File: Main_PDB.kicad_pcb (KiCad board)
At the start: 4 copper layers, 210.1 x 206 mm, 134 parts, among them Q4 NMOS, Q5 NMOS, Q6 NMOS, Q7 NMOS, Q8 NMOS, U10 ACS758LCB-100U-PFF-T, U11 ACS758LCB-100U-PFF-T, U12 ACS758LCB-100U-PFF-T, U2 LM5148RGYR, U3 LMR36015ARNXR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

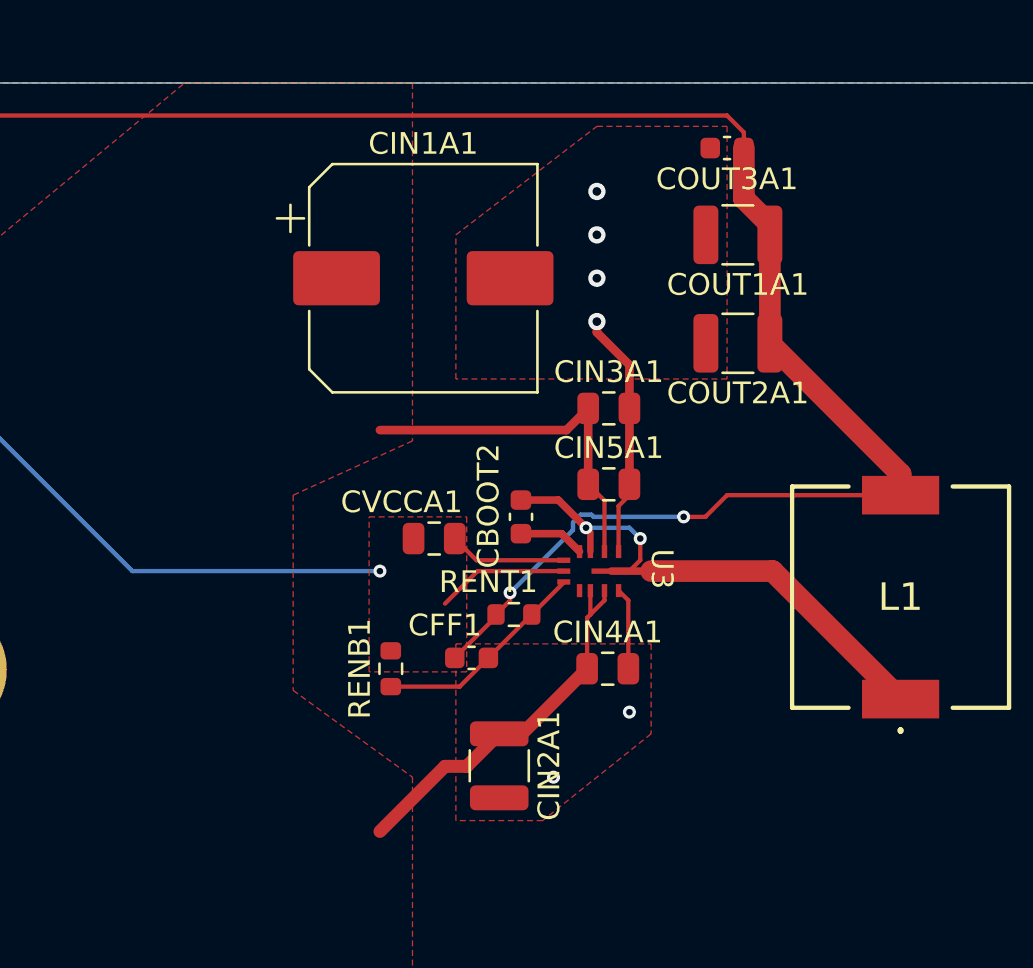
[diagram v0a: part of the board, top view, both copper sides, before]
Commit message: redid 3.3 buck layout on pcb
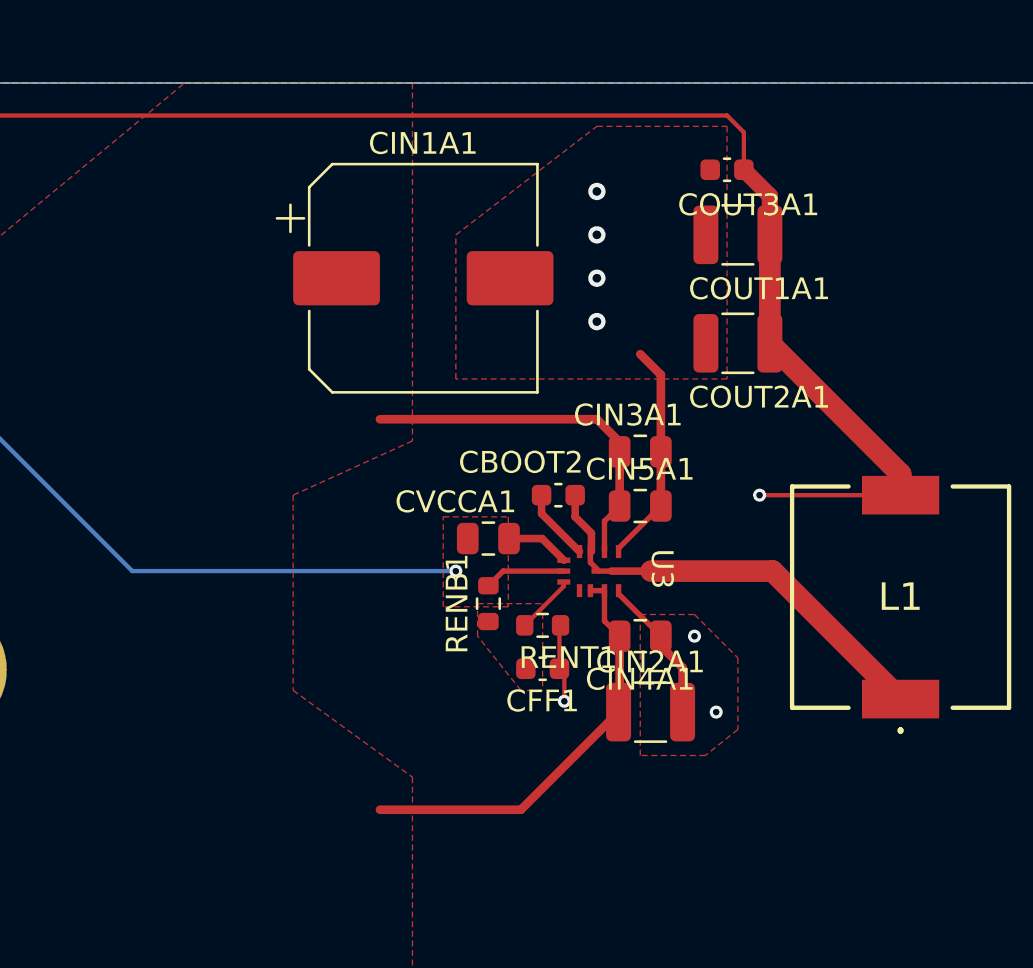
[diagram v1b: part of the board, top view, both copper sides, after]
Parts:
- moved CIN2A1 7.40 mm to (491.5, 73.0), turned to 0 degrees
- moved RENB1 5.41 mm to (484.0, 68.0)
- moved CFF1 3.31 mm to (486.5, 71.0), turned to 180 degrees
- moved CVCCA1 2.50 mm to (484.0, 65.0)
- moved CIN3A1 2.47 mm to (491.0, 61.0)
- moved CIN4A1 2.12 mm to (491.0, 69.5)
- moved CBOOT2 1.99 mm to (487.2, 63.0), turned to 0 degrees
- moved CIN5A1 1.76 mm to (491.0, 63.5)
- moved RENT1 1.42 mm to (486.5, 69.0), turned to 180 degrees
- moved COUT3A1 1.00 mm to (495.0, 48.0)
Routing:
- net Net-(U3-FB): track 9.99 -> 3.06 mm
- net Net-(U3-NC): track 25.7 -> 21.2 mm, vias 2 -> 0
- net +3.3V: track 91.2 -> 94.4 mm
- net Net-(U3-VCC): track 5.44 -> 2.94 mm
- net PGND: track 15.2 -> 17.1 mm
- net /48V_MAIN: track 34.6 -> 36.2 mm
- net AGND: track 47.1 -> 48.3 mm
- added copper zone on F.Cu, net Net-(U3-FB)

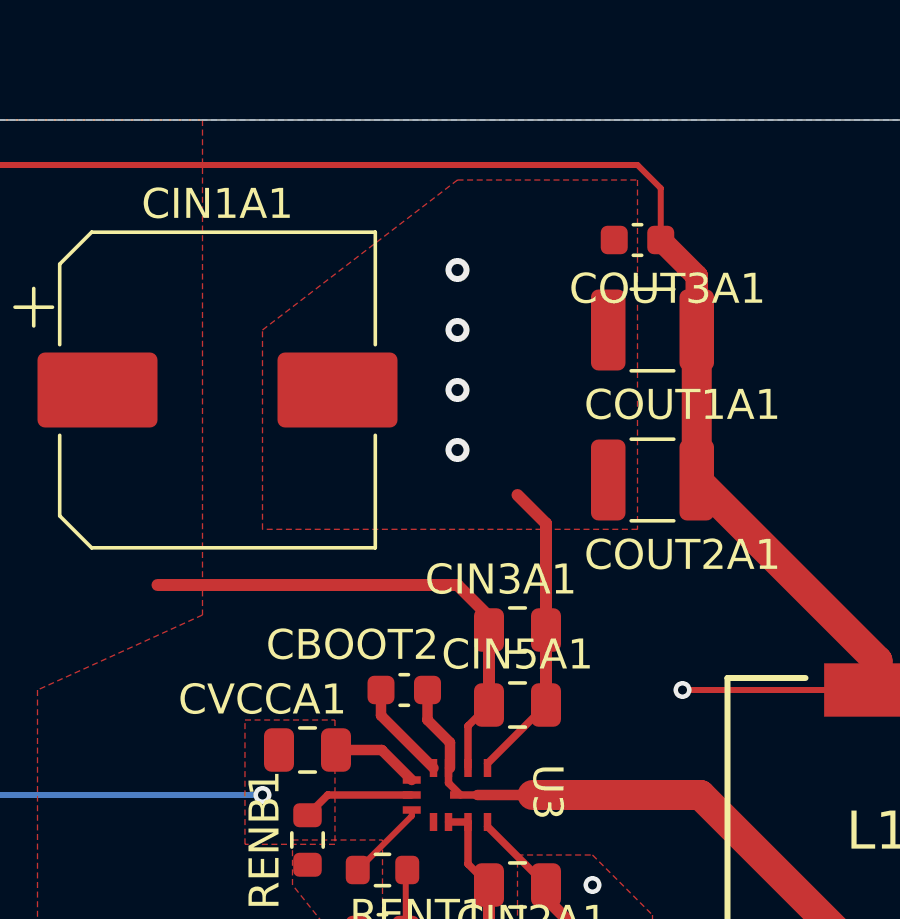
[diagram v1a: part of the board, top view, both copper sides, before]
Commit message: edited pgnd (upper) on 3.3V buck
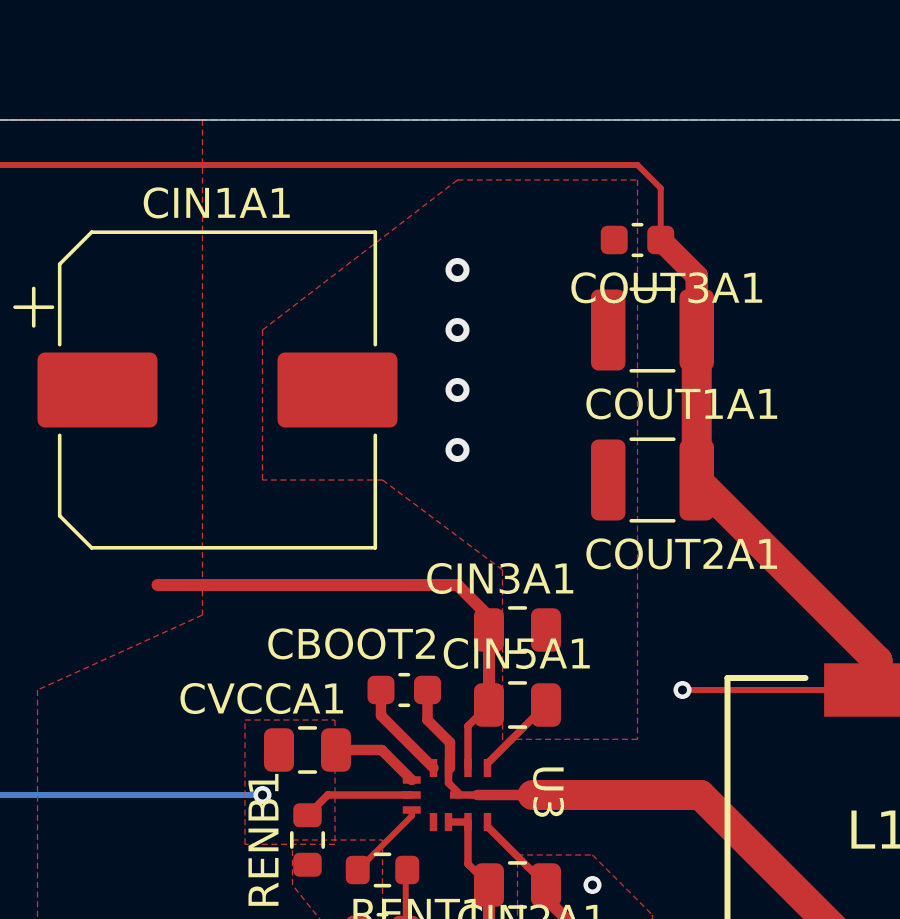
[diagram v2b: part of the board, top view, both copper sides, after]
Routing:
- net PGND: track 17.1 -> 9.73 mm
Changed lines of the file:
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@@
-	)
-	(segment
-		(start 491.95 63.5)
-		(end 491.95 61)
-		(width 0.4)
-		(layer "F.Cu")
-		(net "PGND")
-	)
-	(segment
-		(start 491.95 57.45)
-		(end 491 56.5)
-		(width 0.4)
-		(layer "F.Cu")
-		(net "PGND")
 	)
 	(segment
@@
 	)
 	(segment
-		(start 491.95 61)
-		(end 491.95 57.45)
-		(width 0.4)
-		(layer "F.Cu")
-		(net "PGND")
-	)
-	(segment
 		(start 492.95 70.95)
 		(end 492.95 73)
@@
 		(polygon
 			(pts
-				(xy 495 57.644416) (xy 482.5 57.644416) (xy 482.5 51) (xy 489 46) (xy 495 46)
-			)
-		)
+				(xy 495 64.644416) (xy 490.5 64.644416) (xy 490.504562 64.63794) (xy 490.5 59) (xy 486.5 56) (xy 482.5 56)
+				(xy 482.5 51) (xy 489 46) (xy 495 46)
+			)
+		)

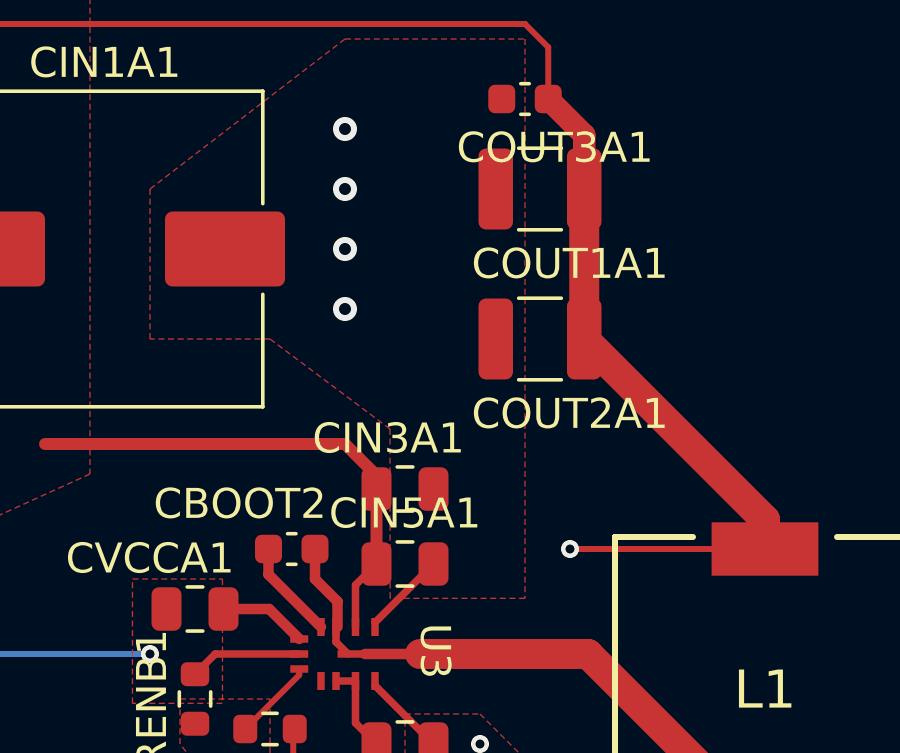
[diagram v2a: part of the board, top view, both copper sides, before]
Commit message: added additonal vias in pgnd pour
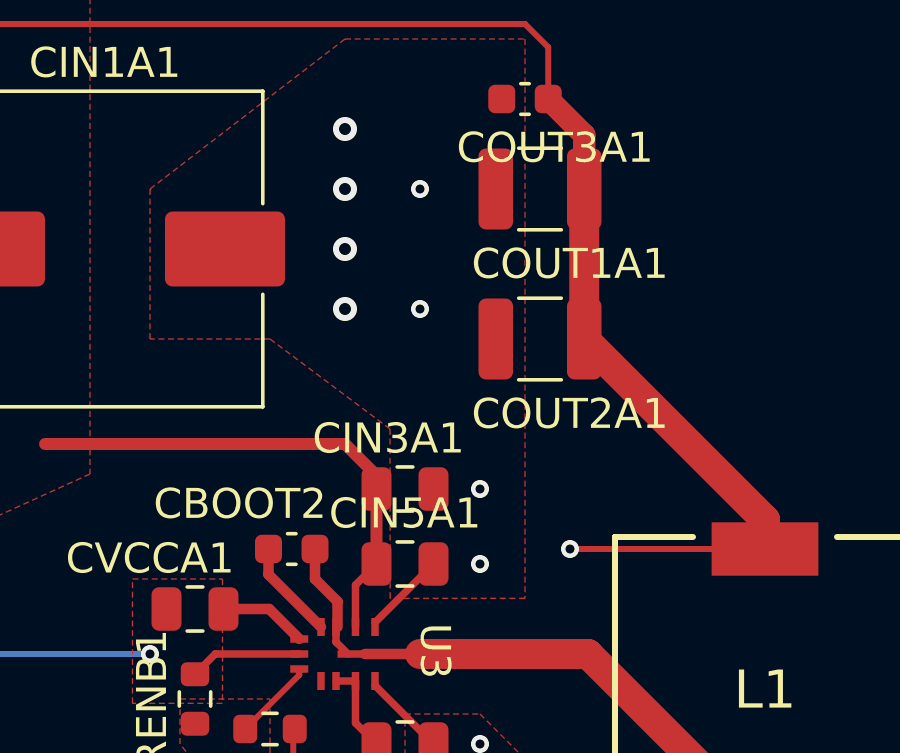
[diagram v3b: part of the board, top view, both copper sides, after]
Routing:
- net PGND: vias 36 -> 40
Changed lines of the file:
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@@
+	)
+	(via
+		(at 491.5 51)
+		(size 0.6)
+		(drill 0.3)
+		(layers "F.Cu" "B.Cu")
+		(free yes)
+		(net "PGND")
 	)
 	(via
@@
 	)
 	(via
+		(at 493.5 61)
+		(size 0.6)
+		(drill 0.3)
+		(layers "F.Cu" "B.Cu")
+		(free yes)
+		(net "PGND")
+	)
+	(via
 		(at 396.5 57.5)
 		(size 1)
@@
 		(size 1)
 		(drill 0.5)
+		(layers "F.Cu" "B.Cu")
+		(free yes)
+		(net "PGND")
+	)
+	(via
+		(at 493.5 63.5)
+		(size 0.6)
+		(drill 0.3)
 		(layers "F.Cu" "B.Cu")
 		(free yes)
@@
 		(layers "F.Cu" "B.Cu")
 		(free yes)
+		(net "PGND")
+	)
+	(via
+		(at 491.5 55)
+		(size 0.6)
+		(drill 0.3)
+		(layers "F.Cu" "B.Cu")
+		(free yes)

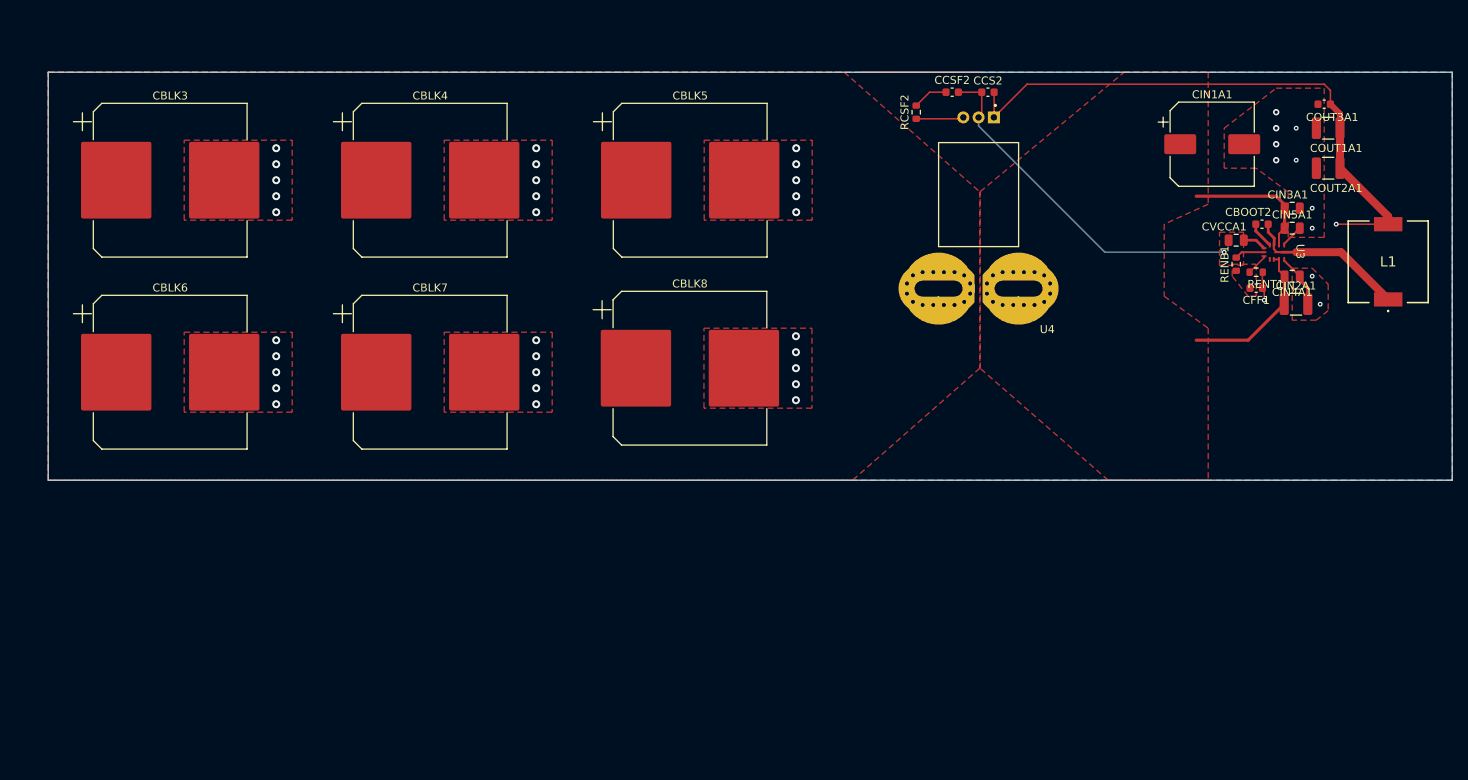
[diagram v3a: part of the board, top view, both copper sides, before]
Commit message: bulk caps relayout and added power pours on bottom layer
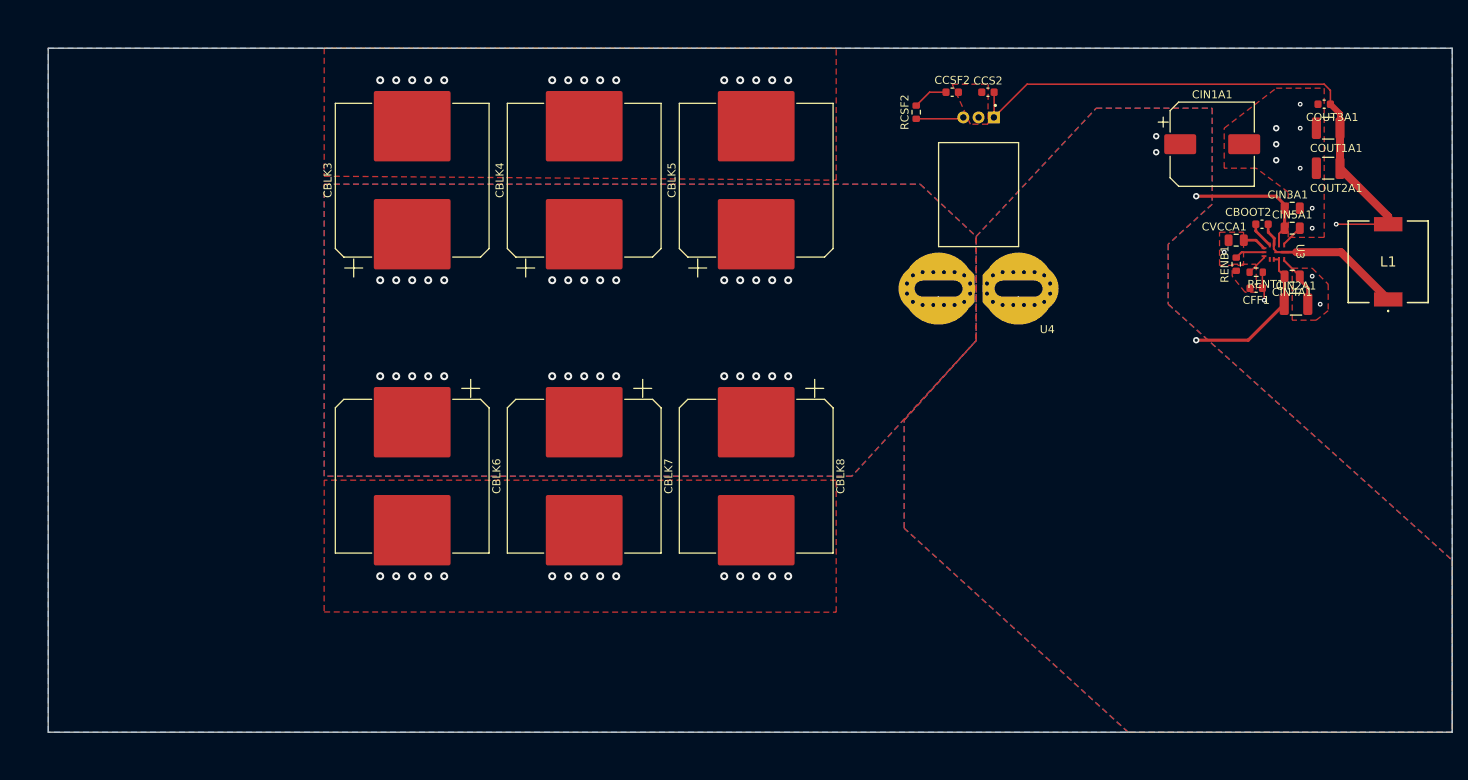
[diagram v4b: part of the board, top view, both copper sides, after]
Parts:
- moved CBLK6 32.9 mm to (381.0, 94.5), turned to -90 degrees
- moved CBLK3 30.2 mm to (381.0, 57.5), turned to 90 degrees
- moved CBLK7 23.2 mm to (402.5, 94.5), turned to -90 degrees
- moved CBLK4 19.2 mm to (402.5, 57.5), turned to 90 degrees
- moved CBLK8 15.8 mm to (424.0, 94.5), turned to -90 degrees
- moved CBLK5 8.25 mm to (424.0, 57.5), turned to 90 degrees
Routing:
- net AGND: track 48.3 -> 42.6 mm
- net /48V_PRECH: vias 0 -> 30
- net /48V_MAIN: vias 0 -> 4
- added copper zone on B.Cu, net /48V_MAIN
- added copper zone on B.Cu, net /48V_PRECH
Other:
- board size 210.1 x 206 mm -> 210.1 x 209 mm

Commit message: silkscreen updates
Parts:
- moved U5 88.4 mm to (133.8, 93.2)
- renumbered CIN4A1 to CHF4A1
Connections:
- CBLK3 pad 2: PGND -> AGND
- CBLK4 pad 2: PGND -> AGND
- CBLK5 pad 2: PGND -> AGND
- CBLK6 pad 2: PGND -> AGND
- CBLK7 pad 2: PGND -> AGND
- CBLK8 pad 2: PGND -> AGND
- CBLKA1 pad 2: PGND -> AGND
- CBLKA2 pad 2: PGND -> AGND
- CBLKA3 pad 2: PGND -> AGND
- CBLKA4 pad 2: PGND -> AGND
- CBULK1 pad 2: PGND -> AGND
- CBULK2 pad 2: PGND -> AGND
- CHF4A1 pad 2: PGND -> AGND
- CIN1A1 pad 2: PGND -> AGND
- CIN1B1 pad 2: PGND -> AGND
- CIN1B2 pad 2: PGND -> AGND
- CIN2A1 pad 2: PGND -> AGND
- CIN2B1 pad 1: PGND -> AGND
- CIN2B2 pad 1: PGND -> AGND
- CIN3A1 pad 2: PGND -> AGND
- CIN3B1 pad 1: PGND -> AGND
- CIN3B2 pad 1: PGND -> AGND
- CIN4B1 pad 1: PGND -> AGND
- CIN4B2 pad 1: PGND -> AGND
- CIN5A1 pad 2: PGND -> AGND
- CIN5B1 pad 1: PGND -> AGND
- CIN5B2 pad 1: PGND -> AGND
- CINC1 pad 1: PGND -> AGND
- CINC10 pad 2: PGND -> AGND
- CINC11 pad 2: PGND -> AGND
- CINC12 pad 2: PGND -> AGND
- CINC2 pad 1: PGND -> AGND
- CINC3 pad 1: PGND -> AGND
- CINC4 pad 1: PGND -> AGND
- CINC5 pad 1: PGND -> AGND
- CINC6 pad 1: PGND -> AGND
- CINC7 pad 1: PGND -> AGND
- CINC8 pad 1: PGND -> AGND
- CINC9 pad 2: PGND -> AGND
- COUT1A1 pad 2: PGND -> AGND
- COUT1B1 pad 2: PGND -> AGND
- COUT1B2 pad 2: PGND -> AGND
- COUT2A1 pad 2: PGND -> AGND
- COUT2B1 pad 2: PGND -> AGND
- COUT2B2 pad 2: PGND -> AGND
- COUT3A1 pad 2: PGND -> AGND
- COUT3B1 pad 2: PGND -> AGND
- COUT3B2 pad 2: PGND -> AGND
- COUT4B1 pad 2: PGND -> AGND
- COUT4B2 pad 2: PGND -> AGND
- CVCC1 pad 2: PGND -> AGND
- CVCC2 pad 2: PGND -> AGND
- D1 pad 2: PGND -> AGND
- D2 pad 2: PGND -> AGND
- D3 pad 2: PGND -> AGND
- D4 pad 2: PGND -> AGND
- D5 pad 2: PGND -> AGND
- D6 pad 2: PGND -> AGND
- D7 pad 2: PGND -> AGND
- D8 pad 2: PGND -> AGND
- Q5 pad 3: PGND -> AGND
- Q6 pad 3: PGND -> AGND
- Q8 pad 3: PGND -> AGND
- RESTOP4 pad 2: PGND -> AGND
- RGND1 pad 1: PGND -> AGND
- U2 pad 10: PGND -> AGND
- U2 pad 25: PGND -> AGND
- U2 pad 7: AGND -> unconnected-(U2-AGND-Pad7)
- U3 pad 1: PGND -> AGND
- U3 pad 11: PGND -> AGND
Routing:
- net PGND: track 9.73 -> 0.00 mm, vias 40 -> 0
- net AGND: track 42.6 -> 52.3 mm, vias 1 -> 41
- added copper zone on B.Cu, net AGND
- added copper zone on In1.Cu, net AGND
- removed copper zone on B.Cu, net (none)
- removed copper zone on F.Cu, net (none)
- removed copper zone on In1.Cu, net (none)
- removed copper zone on B.Cu, net PGND
- removed copper zone on F.Cu, net PGND
- removed copper zone on In1.Cu, net PGND
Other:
- board size 210.1 x 209 mm -> 175.5 x 85.5 mm
- board text removed: "100x100mm placeholder board"
- board text removed: "NOTES: PGND AND AGND POUR SIZES CAN BE ADJUSTED; JUST DRAG THE ZONES lAYER 2 IS GND POURED AND SHOULD NOT HAVE ANY TRACES ON IT. LAYER 4 IS ALSO GND POURED BUT TRACES MAY BE RUN ON IT lAYER 3 IS THE QUIETEST LAYER, IF YOU CANTRY TO RUN MOST SENSITIVE TRACES HERE. SIMILARLY TRY TO RUN NOISIEST TRACES ON LAYER 1"
